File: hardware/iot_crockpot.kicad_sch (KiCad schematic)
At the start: 27 parts, among them J1 Screw_Terminal_01x02, J2 Screw_Terminal_01x02, J3 Screw_Terminal_01x02, J4 Conn_01x04_Pin, J5 Conn_01x04_Pin, J6 Conn_ARM_SWD_TagConnect_TC2030, K1 G5LE-14 5VDC, K2 G5LE-14 5VDC, Q1 2N7002, Q2 2N7002, U1 STM32G031F6Px, U3 MAX31855KASA

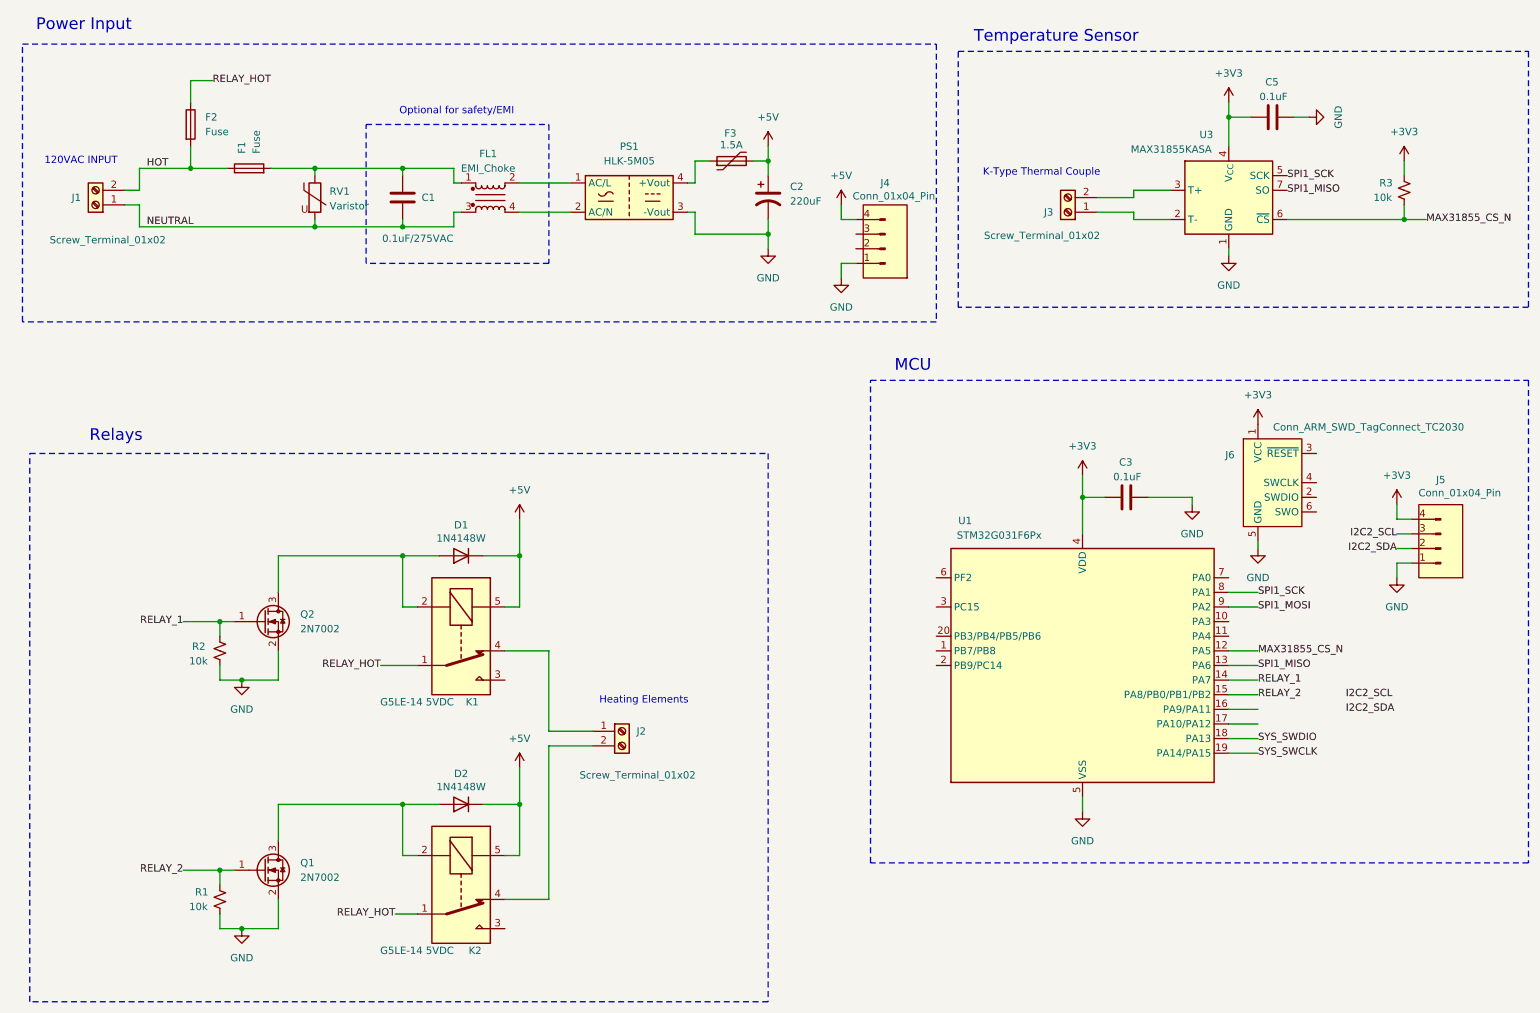
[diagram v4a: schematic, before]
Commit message: Begin schematic rework for single-board ESP32-S3 design
- Split KiCad schematic into hierarchical sheets (MCU + power/relay/tempsens)
- Add docs/schematic_rework_plan.md: step-by-step guide for reworking the
  schematic from the old CYD+STM32 two-board design to the new ESP32-S3
  single-board design
- Update all READMEs to reflect finalized single-board architecture:
  - firmware/README.md: rewrite for ESP32-S3 target, correct GPIO table
  - hardware/README.md: rewrite for single-board design, schematic status
  - README.md: update hardware checklist, add schematic_rework_plan to docs
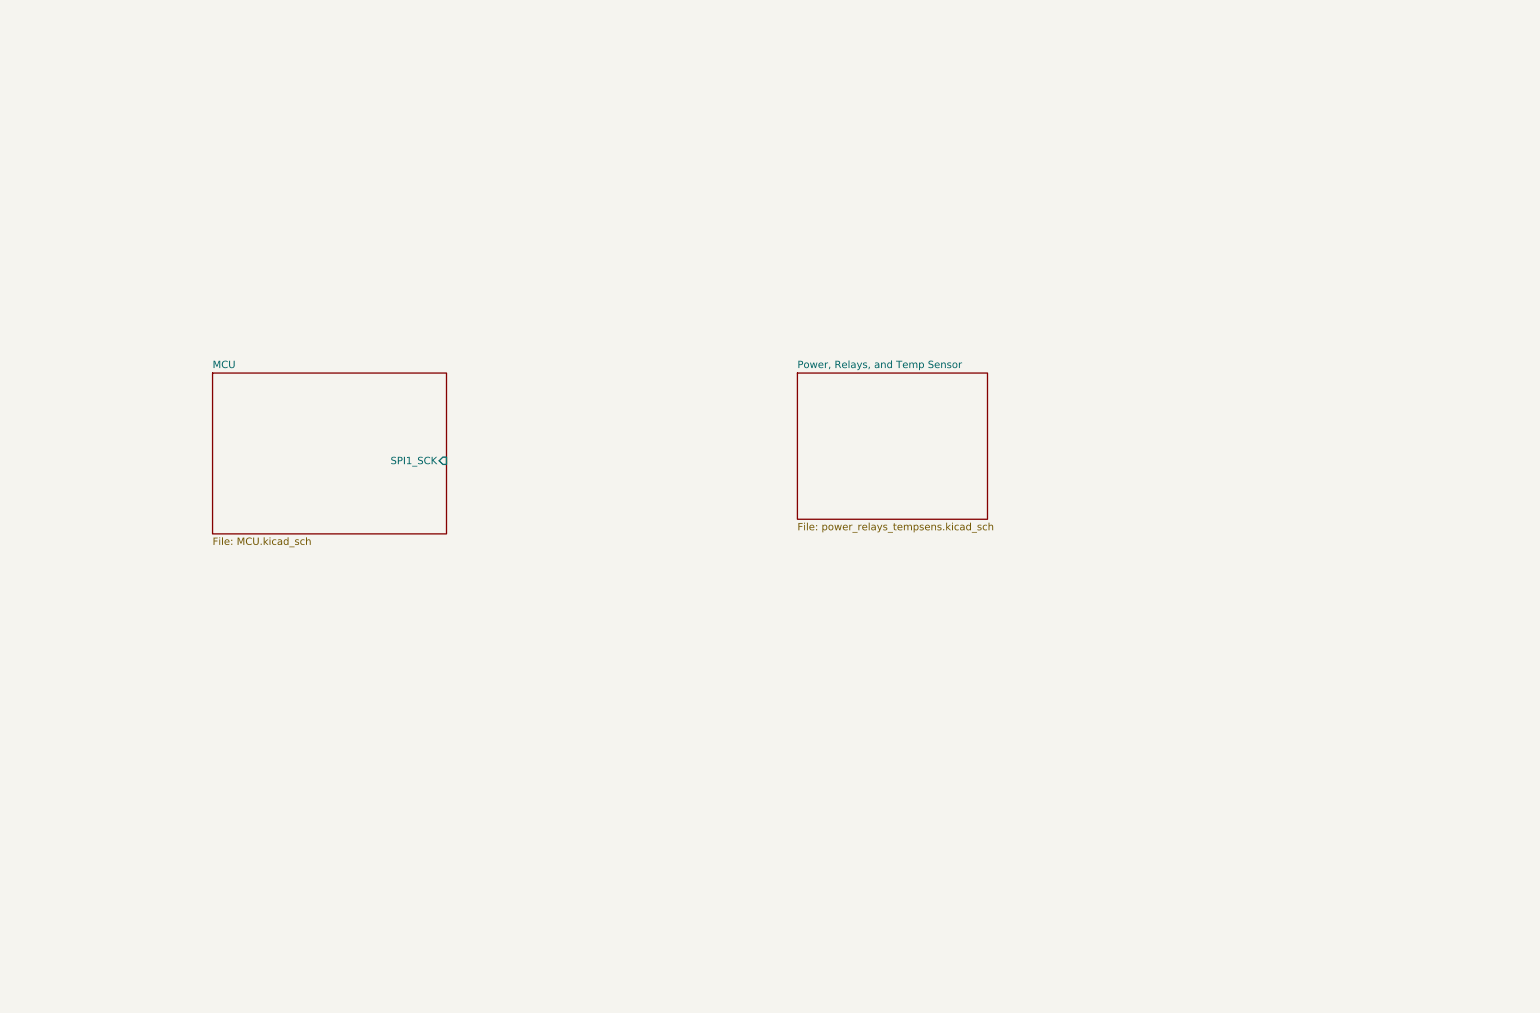
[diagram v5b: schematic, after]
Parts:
- removed C1: 0.1uF/275VAC, symbol Device:C
- removed C2: 220uF, symbol Device:C_Polarized_US
- removed C3, C5: 0.1uF, Capacitor_SMD:C_0603_1608Metric_Pad1.08x0.95mm_HandSolder, symbol Device:C
- removed D1, D2: 1N4148W, Diode_SMD:D_SOD-123, symbol Diode:1N4148W
- removed F1: Fuse, Fuses:Fuseholder_Clip-5x20mm_Littelfuse_111_Inline_P20.00x5.00mm_D1.05mm_Horizontal_with_3D_body, symbol Device:Fuse
- removed F2: Fuse, symbol Device:Fuse
- removed F3: 1.5A, Fuse:Fuse_1206_3216Metric_Pad1.42x1.75mm_HandSolder, symbol Device:Polyfuse
- removed FL1: EMI_Choke, symbol Device:Filter_EMI_CommonMode
- removed J1, J2, J3: Screw_Terminal_01x02, TerminalBlock_Phoenix:TerminalBlock_Phoenix_MKDS-1,5-2_1x02_P5.00mm_Horizontal, symbol Connector:Screw_Terminal_01x02
- removed J4, J5: Conn_01x04_Pin, symbol Connectors:Conn_01x04_Pin
- removed J6: Conn_ARM_SWD_TagConnect_TC2030, Connector:Tag-Connect_TC2030-IDC-FP_2x03_P1.27mm_Vertical, symbol Connector:Conn_ARM_SWD_TagConnect_TC2030
- removed K1, K2: G5LE-14 5VDC, Relay_THT:Relay_SPDT_Omron-G5LE-1, symbol Relay:G5LE-1
- removed PS1: HLK-5M05, Converter_ACDC:Converter_ACDC_Hi-Link_HLK-5Mxx, symbol Converter_ACDC:HLK-5M05
- removed Q1, Q2: 2N7002, Package_TO_SOT_SMD:SOT-23, symbol Transistor_FET:2N7002
- removed R1, R2, R3: 10k, Resistor_SMD:R_0603_1608Metric, symbol Device:R_Small_US
- removed RV1: Varistor, Varistor:RV_Rect_V25S440P_L26.5mm_W8.2mm_P12.7mm, symbol Device:Varistor
- removed U1: STM32G031F6Px, Package_SO:TSSOP-20_4.4x6.5mm_P0.65mm, symbol MCU_ST_STM32G0:STM32G031F6Px
- removed U3: MAX31855KASA, Package_SO:SOIC-8_3.9x4.9mm_P1.27mm, symbol Sensor_Temperature:MAX31855KASA
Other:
- added sheet MCU (MCU.kicad_sch)
- added sheet Power, Relays, and Temp Sensor (power_relays_tempsens.kicad_sch)
- note removed: "120VAC INPUT"
- note removed: "Heating Elements"
- note removed: "K-Type Thermal Couple"
- note removed: "MCU"
- note removed: "Optional for safety/EMI"
- note removed: "Power Input"
- note removed: "Relays"
- note removed: "Temperature Sensor"
